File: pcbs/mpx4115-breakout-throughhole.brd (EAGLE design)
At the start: 13 x 13.5 mm, 5 parts

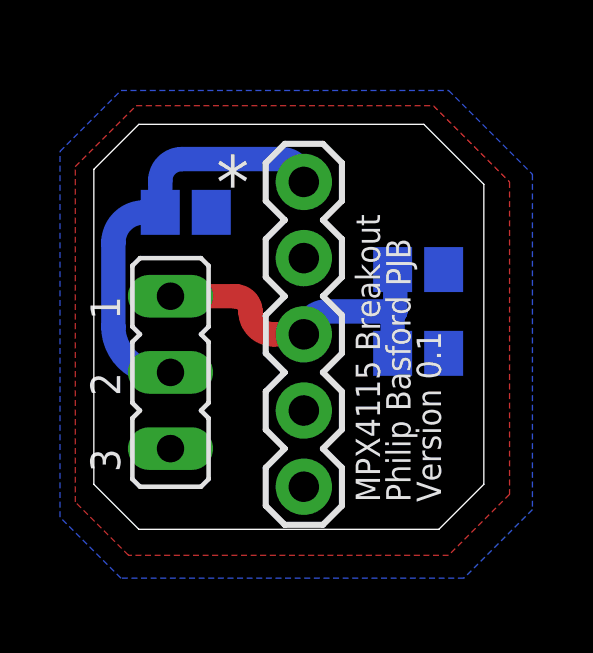
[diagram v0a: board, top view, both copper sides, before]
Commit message: now with 6 holes for pressure sensor
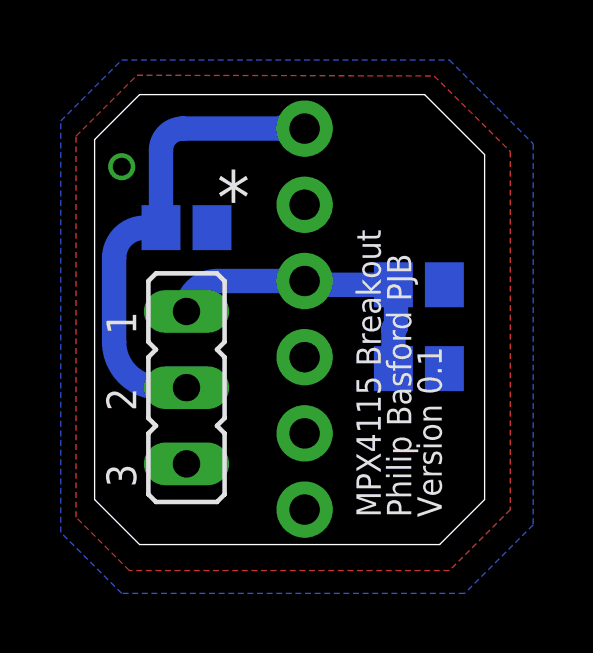
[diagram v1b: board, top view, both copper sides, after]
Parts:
- JP2: device SparkFun-Connectors:1X05 -> SparkFun-Connectors:1X06_NO_SILK
- moved JP2 1.78 mm to (0.03, 6.86)
- moved JP1 0.74 mm to (-3.91, -1.78)
- moved C2 0.51 mm to (3.84, -1.14)
- moved C3 0.51 mm to (-3.91, 3.56)
- moved C1 0.51 mm to (3.84, 1.65)
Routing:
- net VOUT: track 13.8 -> 15.5 mm
- net VCC: track 11.2 -> 10.2 mm
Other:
- board size 13 x 13.5 mm -> 13 x 15 mm
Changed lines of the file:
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@@
 <setting verticaltext="up"/>
 </settings>
-<grid distance="10" unitdist="mil" unit="mil" style="lines" multiple="1" display="yes" altdistance="0.025" altunitdist="inch" altunit="inch"/>
+<grid distance="10" unitdist="mil" unit="mil" style="lines" multiple="1" display="yes" altdistance="1" altunitdist="mil" altunit="mil"/>
 <layers>
 <layer number="1" name="Top" color="4" fill="1" visible="yes" active="yes"/>
@@
 <board>
 <plain>
-<text x="-2.921" y="4.191" size="1.778" layer="25" font="vector">*</text>
-<wire x1="-5.5" y1="7" x2="4" y2="7" width="0" layer="20"/>
-<wire x1="4" y1="7" x2="6" y2="5" width="0" layer="20"/>
-<wire x1="6" y1="5" x2="6" y2="-5" width="0" layer="20"/>
-<wire x1="6" y1="-5" x2="4.5" y2="-6.5" width="0" layer="20"/>
-<wire x1="4.5" y1="-6.5" x2="-5.5" y2="-6.5" width="0" layer="20"/>
-<wire x1="-5.5" y1="-6.5" x2="-7" y2="-5" width="0" layer="20"/>
-<wire x1="-7" y1="-5" x2="-7" y2="5.5" width="0" layer="20"/>
-<wire x1="-7" y1="5.5" x2="-5.5" y2="7" width="0" layer="20"/>
-<text x="2.54" y="-5.588" size="0.8128" layer="25" font="vector" rot="R90">MPX4115 Breakout</text>
-<text x="3.556" y="-5.588" size="0.8128" layer="25" font="vector" rot="R90">Philip Basford PJB</text>
-<text x="4.572" y="-5.588" size="0.8128" layer="25" font="vector" rot="R90">Version 0.1</text>
+<text x="-2.8956" y="3.683" size="1.778" layer="25" font="vector">*</text>
+<wire x1="-5.4746" y1="7.9906" x2="4.0254" y2="7.9906" width="0" layer="20"/>
+<wire x1="4.0254" y1="7.9906" x2="6.0254" y2="5.9906" width="0" layer="20"/>
+<wire x1="6.0254" y1="5.9906" x2="6.0254" y2="-5.508" width="0" layer="20"/>
+<wire x1="6.0254" y1="-5.508" x2="4.5254" y2="-7.008" width="0" layer="20"/>
+<wire x1="4.5254" y1="-7.008" x2="-5.4746" y2="-7.008" width="0" layer="20"/>
+<wire x1="-5.4746" y1="-7.008" x2="-6.9746" y2="-5.508" width="0" layer="20"/>
+<wire x1="-6.9746" y1="-5.508" x2="-6.9746" y2="6.4906" width="0" layer="20"/>
+<wire x1="-6.9746" y1="6.4906" x2="-5.4746" y2="7.9906" width="0" layer="20"/>
+<text x="2.5654" y="-6.096" size="0.8128" layer="25" font="vector" rot="R90">MPX4115 Breakout</text>
+<text x="3.5814" y="-6.096" size="0.8128" layer="25" font="vector" rot="R90">Philip Basford PJB</text>
+<text x="4.5974" y="-6.096" size="0.8128" layer="25" font="vector" rot="R90">Version 0.1</text>
 </plain>
 <attributes>
@@
 </autorouter>
 <elements>
-<element name="JP1" library="jumper" package="JP2" value="" x="-4.445" y="-1.27" smashed="yes" rot="R270">
-<attribute name="VALUE" x="-8.763" y="2.286" size="1.27" layer="27" ratio="10" rot="R270"/>
+<element name="JP1" library="jumper" package="JP2" value="" x="-3.9116" y="-1.778" smashed="yes" rot="R270">
+<attribute name="VALUE" x="-8.2296" y="1.778" size="1.27" layer="27" ratio="10" rot="R270"/>
 </element>
-<element name="C1" library="resistor" package="C0805" value="1uF" x="3.81" y="2.159" smashed="yes" rot="MR180">
-<attribute name="NAME" x="2.921" y="4.699" size="1.27" layer="26" rot="MR180"/>
+<element name="C1" library="resistor" package="C0805" value="1uF" x="3.8354" y="1.651" smashed="yes" rot="MR180">
+<attribute name="NAME" x="2.9464" y="4.191" size="1.27" layer="26" rot="MR180"/>
 </element>
-<element name="C2" library="resistor" package="C0805" value="10nF" x="3.81" y="-0.635" smashed="yes" rot="MR180">
-<attribute name="NAME" x="3.175" y="-2.159" size="1.27" layer="26" rot="MR180"/>
+<element name="C2" library="resistor" package="C0805" value="10nF" x="3.8354" y="-1.143" smashed="yes" rot="MR180">
+<attribute name="NAME" x="3.2004" y="-2.667" size="1.27" layer="26" rot="MR180"/>
 </element>
-<element name="C3" library="resistor" package="C0805" value="470pF" x="-3.937" y="4.064" smashed="yes" rot="MR180">
-<attribute name="NAME" x="-4.572" y="6.604" size="1.27" layer="26" rot="MR180"/>
+<element name="C3" library="resistor" package="C0805" value="470pF" x="-3.9116" y="3.556" smashed="yes" rot="MR180">
+<attribute name="NAME" x="-4.5466" y="7.62" size="1.27" layer="26" rot="MR180"/>
 </element>
-<element name="JP2" library="SparkFun-Connectors" package="1X05" value="" x="0" y="5.08" smashed="yes" rot="R270">
-<attribute name="VALUE" x="-3.175" y="6.35" size="1.27" layer="27" rot="R270"/>
+<element name="JP2" library="SparkFun-Connectors" package="1X06_NO_SILK" value="" x="0.0254" y="6.858" smashed="yes" rot="R270">
+<attribute name="VALUE" x="-3.1496" y="8.128" size="1.27" layer="27" rot="R270"/>
 </element>
 </elements>
@@
 <contactref element="JP2" pad="2"/>
 <polygon width="0.1524" layer="16">
-<vertex x="-6.096" y="8.128"/>
-<vertex x="4.826" y="8.128"/>
-<vertex x="7.62" y="5.334"/>
-<vertex x="7.62" y="-5.842"/>
-<vertex x="5.334" y="-8.128"/>
-<vertex x="-6.096" y="-8.128"/>
-<vertex x="-8.128" y="-6.096"/>
-<vertex x="-8.128" y="6.096"/>
+<vertex x="-6.0706" y="9.144"/>
+<vertex x="4.8514" y="9.144"/>
+<vertex x="7.6454" y="6.35"/>
+<vertex x="7.6454" y="-6.35"/>
+<vertex x="5.3594" y="-8.636"/>
+<vertex x="-6.0706" y="-8.636"/>
+<vertex x="-8.1026" y="-6.604"/>
+<vertex x="-8.1026" y="7.112"/>
 </polygon>
 <polygon width="0.1524" layer="1">
-<vertex x="-5.588" y="7.62"/>
-<vertex x="4.318" y="7.62"/>
-<vertex x="6.858" y="5.08"/>
-<vertex x="6.858" y="-5.334"/>
-<vertex x="4.826" y="-7.366"/>
-<vertex x="-5.842" y="-7.366"/>
-<vertex x="-7.62" y="-5.588"/>
-<vertex x="-7.62" y="5.588"/>
+<vertex x="-5.5626" y="8.636"/>
+<vertex x="4.3434" y="8.6106"/>
+<vertex x="6.8834" y="6.096"/>
+<vertex x="6.8834" y="-5.842"/>
+<vertex x="4.8514" y="-7.874"/>
+<vertex x="-5.8166" y="-7.874"/>
+<vertex x="-7.5946" y="-6.096"/>
+<vertex x="-7.5946" y="6.604"/>
 </polygon>
+<via x="-6.0706" y="5.588" extent="1-16" drill="0.6" shape="square"/>
 </signal>
 <signal name="VCC">
@@
 <contactref element="C1" pad="1"/>
 <contactref element="C2" pad="1"/>
-<wire x1="-4.445" y1="1.27" x2="-2.286" y2="1.27" width="0.8128" layer="1"/>
-<wire x1="-2.286" y1="1.27" x2="-1.778" y2="0.762" width="0.8128" layer="1" curve="-90"/>
-<wire x1="-1.778" y1="0.762" x2="-1.016" y2="0" width="0.8128" layer="1" curve="90"/>
-<wire x1="-1.016" y1="0" x2="0" y2="0" width="0.8128" layer="1"/>
-<wire x1="0" y1="0" x2="0.762" y2="0.762" width="0.8128" layer="16" curve="-90"/>
-<wire x1="0.762" y1="0.762" x2="3.048" y2="0.762" width="0.8128" layer="16"/>
-<wire x1="3.048" y1="0.762" x2="2.96" y2="0.674" width="0.8128" layer="16" curve="90"/>
-<wire x1="2.96" y1="0.674" x2="2.96" y2="-0.635" width="0.8128" layer="16"/>
-<wire x1="2.96" y1="2.159" x2="3.048" y2="2.071" width="0.8128" layer="16" curve="-90"/>
-<wire x1="3.048" y1="2.071" x2="3.048" y2="0.762" width="0.8128" layer="16"/>
+<wire x1="3.0734" y1="0.254" x2="2.9854" y2="0.166" width="0.8128" layer="16" curve="90"/>
+<wire x1="2.9854" y1="0.166" x2="2.9854" y2="-1.143" width="0.8128" layer="16"/>
+<wire x1="2.9854" y1="1.651" x2="3.0734" y2="1.563" width="0.8128" layer="16" curve="-90"/>
+<wire x1="3.0734" y1="1.563" x2="3.0734" y2="0.254" width="0.8128" layer="16"/>
+<wire x1="-3.9116" y1="0.762" x2="-2.8956" y2="1.778" width="0.8128" layer="16" curve="-90"/>
+<wire x1="-2.8956" y1="1.778" x2="0.0254" y2="1.778" width="0.8128" layer="16"/>
+<wire x1="0.0254" y1="1.778" x2="0.1524" y2="1.651" width="0.8128" layer="16" curve="90"/>
+<wire x1="0.1524" y1="1.651" x2="2.9854" y2="1.651" width="0.8128" layer="16"/>
 </signal>
 <signal name="VOUT">
@@
 <contactref element="C3" pad="1"/>
 <contactref element="JP2" pad="1"/>
-<wire x1="-4.445" y1="-1.27" x2="-4.826" y2="-1.27" width="0.8128" layer="16"/>
-<wire x1="-4.826" y1="-1.27" x2="-6.35" y2="0.254" width="0.8128" layer="16" curve="-90"/>
-<wire x1="-6.35" y1="0.254" x2="-6.35" y2="3.048" width="0.8128" layer="16"/>
-<wire x1="-6.35" y1="3.048" x2="-5.334" y2="4.064" width="0.8128" layer="16" curve="-90"/>
-<wire x1="-5.334" y1="4.064" x2="-4.787" y2="4.064" width="0.8128" layer="16"/>
-<wire x1="-4.787" y1="4.064" x2="-4.787" y2="5.119" width="0.8128" layer="16"/>
-<wire x1="-4.787" y1="5.119" x2="-4.064" y2="5.842" width="0.8128" layer="16" curve="-90"/>
-<wire x1="-4.064" y1="5.842" x2="-0.762" y2="5.842" width="0.8128" layer="16"/>
-<wire x1="-0.762" y1="5.842" x2="0" y2="5.08" width="0.8128" layer="16" curve="-90"/>
+<wire x1="-3.9116" y1="-1.778" x2="-4.8006" y2="-1.778" width="0.8128" layer="16"/>
+<wire x1="-4.8006" y1="-1.778" x2="-6.3246" y2="-0.254" width="0.8128" layer="16" curve="-90"/>
+<wire x1="-6.3246" y1="-0.254" x2="-6.3246" y2="2.54" width="0.8128" layer="16"/>
+<wire x1="-6.3246" y1="2.54" x2="-5.3086" y2="3.556" width="0.8128" layer="16" curve="-90"/>
+<wire x1="-5.3086" y1="3.556" x2="-4.7616" y2="3.556" width="0.8128" layer="16"/>
+<wire x1="-4.7616" y1="3.556" x2="-4.7616" y2="6.135" width="0.8128" layer="16"/>
+<wire x1="-4.7616" y1="6.135" x2="-4.0386" y2="6.858" width="0.8128" layer="16" curve="-90"/>
+<wire x1="-4.0386" y1="6.858" x2="-0.7366" y2="6.858" width="0.8128" layer="16"/>
+<wire x1="-0.7366" y1="6.858" x2="0.0254" y2="6.858" width="0.8128" layer="16" curve="-90"/>
 </signal>
 <signal name="N$3">
